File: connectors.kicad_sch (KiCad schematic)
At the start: 15 parts, among them J1 Compute-Module-4_Plug_Connect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, Q2 SQS401EN-T1_BE3, Q3 DZDH0401DW, U20 NTS0102_XSON, U21 NTS0102_XSON

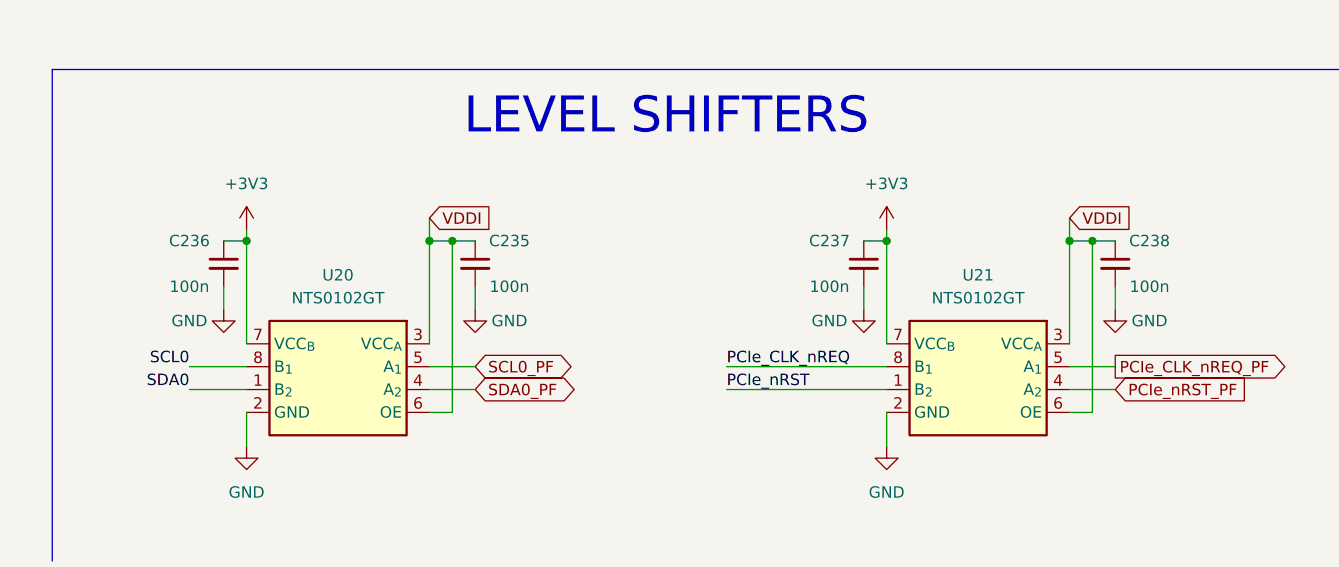
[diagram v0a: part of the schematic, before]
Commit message: [#55992] Replace 100n capacitors
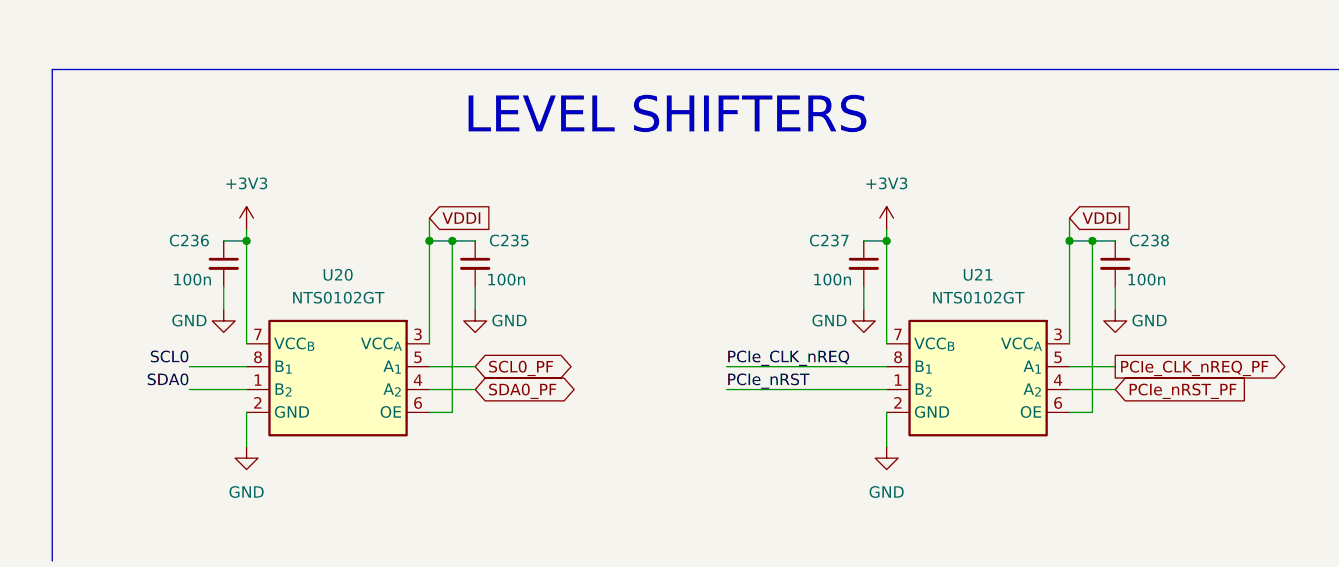
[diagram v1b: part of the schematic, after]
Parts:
- C235, C236, C237, C238: value C_100n_0201 -> C_100n_0402; footprint antmicro-footprints:C_0201 -> antmicro-footprints:C_0402_1005Metric; symbol antmicroCapacitorsmisc:C_100n_0201 -> antmicroCapacitors0402:C_100n_0402; Dielectric (none) -> X5R; MPN CC0201KRX6S5BB104 -> GRM155R61H104KE14D; Manufacturer YAGEO -> Murata; Voltage (none) -> 50V

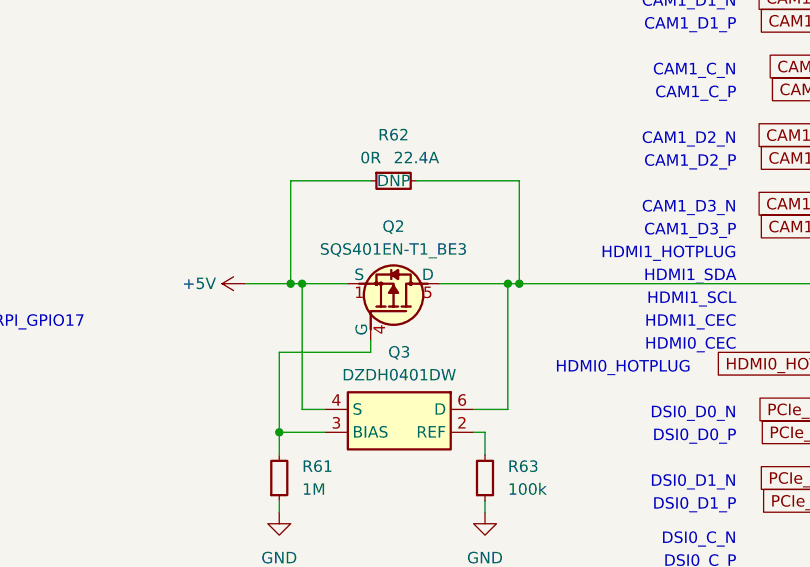
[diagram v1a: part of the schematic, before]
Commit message: [#56060] Connect power monitor and ideal diode
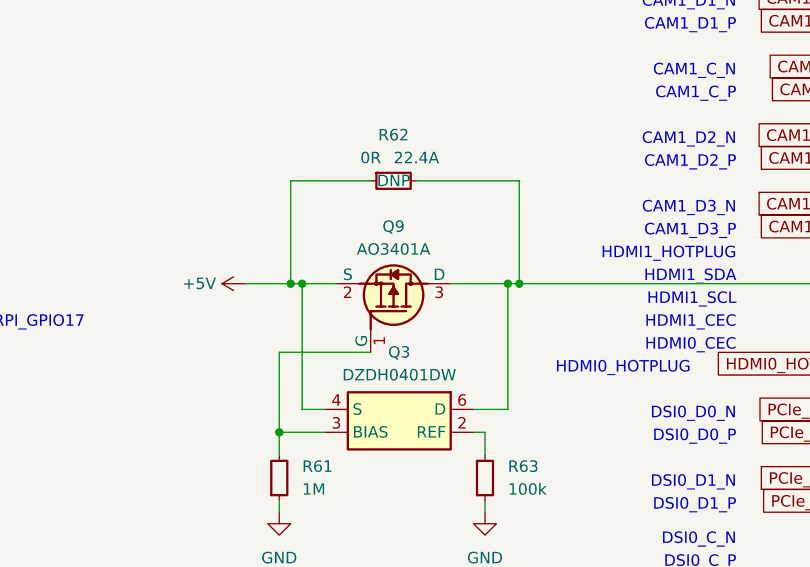
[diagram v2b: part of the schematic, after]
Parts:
- removed Q2: SQS401EN-T1_BE3, antmicro-footprints:Vishay_PowerPAK_1212-8_Single, symbol antmicroTransistorsFETsMOSFETsSingle:SQS401EN-T1_BE3
- added Q9: AO3401A, antmicro-footprints:SOT-23-3, symbol antmicroTransistorsFETsMOSFETsSingle:AO3401A
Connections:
- net +5V: now also Q9.2 (S)
- net at Q3.3 (BIAS), R61.2: now also Q9.1 (G)
- net at J1.143, J1.145, J1.147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: now also Q9.3 (D)
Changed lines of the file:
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@@
     (stroke (width 0) (type default))
   )
-  (wire (pts (xy 234.95 135.89) (xy 242.57 135.89))
-    (stroke (width 0) (type default))
-  )
   (wire (pts (xy 124.46 81.28) (xy 129.54 81.28))
     (stroke (width 0) (type default))
@@
     (stroke (width 0) (type default))
   )
+  (wire (pts (xy 236.22 135.89) (xy 242.57 135.89))
+    (stroke (width 0) (type default))
+  )
   (wire (pts (xy 220.98 247.65) (xy 220.98 259.08))
     (stroke (width 0) (type default))
@@
     (stroke (width 0) (type default))
   )
-  (wire (pts (xy 227.33 142.24) (xy 227.33 143.51))
-    (stroke (width 0) (type default))
-  )
   (wire (pts (xy 133.35 177.8) (xy 124.46 177.8))
     (stroke (width 0) (type default))
@@
     (stroke (width 0) (type default))
   )
-  (wire (pts (xy 219.71 135.89) (xy 224.79 135.89))
+  (wire (pts (xy 219.71 135.89) (xy 223.52 135.89))
     (stroke (width 0) (type default))
   )
@@
     )
   )
-  (symbol (lib_id "antmicroTransistorsFETsMOSFETsSingle:SQS401EN-T1_BE3") (at 227.33 142.24 270) (mirror x) (unit 1)
-    (in_bom no) (on_board yes) (dnp no)
-    (property "Reference" "Q2" (at 229.87 129.54 90)
-      (effects (font (size 1.27 1.27) (thickness 0.15)))
-    )
-    (property "Value" "SQS401EN-T1_BE3" (at 217.17 127 0)
-      (effects (font (size 1.27 1.27) (thickness 0.15)) (justify left bottom) hide)
-    )
-    (property "Footprint" "antmicro-footprints:Vishay_PowerPAK_1212-8_Single" (at 214.63 127 0)
-      (effects (font (size 1.27 1.27) (thickness 0.15)) (justify left bottom) hide)
-    )
-    (property "Datasheet" "https://www.vishay.com/docs/65529/sqs401en.pdf" (at 212.09 127 0)
-      (effects (font (size 1.27 1.27) (thickness 0.15)) (justify left bottom) hide)
-    )
-    (property "MPN" "SQS401EN-T1_BE3" (at 229.87 132.08 90)
-      (effects (font (size 1.27 1.27) (thickness 0.15)))
-    )
-    (property "Manufacturer" "Vishay" (at 209.55 127 0)
-      (effects (font (size 1.27 1.27) (thickness 0.15)) (justify left bottom) hide)
-    )
-    (property "Author" "Antmicro" (at 207.01 127 0)
-      (effects (font (size 1.27 1.27) (thickness 0.15)) (justify left bottom) hide)
-    )
-    (property "License" "Apache-2.0" (at 204.47 127 0)
-      (effects (font (size 1.27 1.27) (thickness 0.15)) (justify left bottom) hide)
-    )
-    (pin "3")
-    (pin "1")
-    (pin "4")
-    (pin "2")
-    (pin "5")
-    (instances
-      (project "polarfire-som"
-        (path "/db4a0d3e-2eb3-499e-977d-6eb378cfd3ed/1a89b4c6-5d95-4c13-8da9-62b42c0a8ed9"
-          (reference "Q2") (unit 1)
-        )
-      )
-    )
-  )
   (symbol (lib_id "antmicroResistors0603:R_10k_0603") (at 165.1 140.97 0) (unit 1)
     (in_bom yes) (on_board yes) (dnp no)
@@
         )
       )
+    )
+  )
+  (symbol (lib_id "antmicroTransistorsFETsMOSFETsSingle:AO3401A") (at 227.33 143.51 270) (mirror x) (unit 1)
+    (in_bom yes) (on_board yes) (dnp no)
+    (property "Reference" "Q9" (at 229.87 129.54 90)
+      (effects (font (size 1.27 1.27) (thickness 0.15)))
+    )
+    (property "Value" "AO3401A" (at 229.87 132.08 90)
+      (effects (font (size 1.27 1.27) (thickness 0.15)))
+    )
+    (property "Footprint" "antmicro-footprints:SOT-23-3" (at 215.9 120.65 0)
+      (effects (font (size 1.27 1.27) (thickness 0.15)) (justify left bottom) hide)
+    )
+    (property "Datasheet" "http://aosmd.com/res/data_sheets/AO3401A.pdf" (at 213.36 120.65 0)
+      (effects (font (size 1.27 1.27) (thickness 0.15)) (justify left bottom) hide)
+    )
+    (property "MPN" "AO3401A" (at 210.82 120.65 0)
+      (effects (font (size 1.27 1.27) (thickness 0.15)) (justify left bottom) hide)
+    )
+    (property "Manufacturer" "AOSMD" (at 208.28 120.65 0)
+      (effects (font (size 1.27 1.27) (thickness 0.15)) (justify left bottom) hide)
+    )
+    (property "Author" "Antmicro" (at 205.74 120.65 0)
+      (effects (font (size 1.27 1.27) (thickness 0.15)) (justify left bottom) hide)
+    )
+    (property "License" "Apache-2.0" (at 203.2 120.65 0)
+      (effects (font (size 1.27 1.27) (thickness 0.15)) (justify left bottom) hide)
+    )
+    (pin "2")
+    (pin "1")
+    (pin "3")
+    (instances
+      (project "polarfire-som"
+        (path "/db4a0d3e-2eb3-499e-977d-6eb378cfd3ed/1a89b4c6-5d95-4c13-8da9-62b42c0a8ed9"
+          (reference "Q9") (unit 1)
+        )
+      )

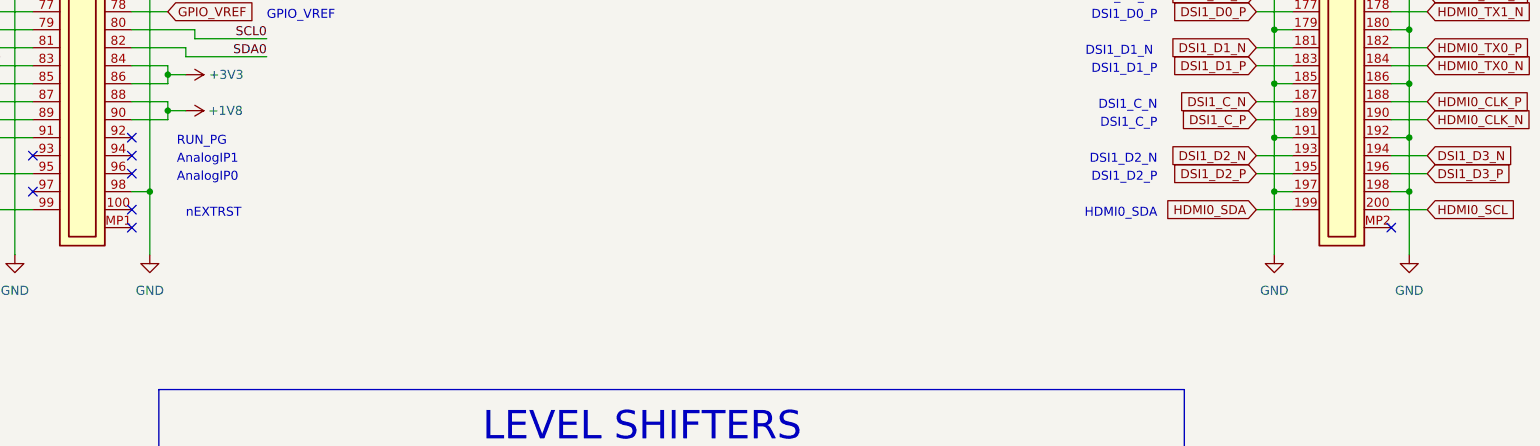
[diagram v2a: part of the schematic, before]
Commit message: [#56060] Finish PDN, continue routing LS signals
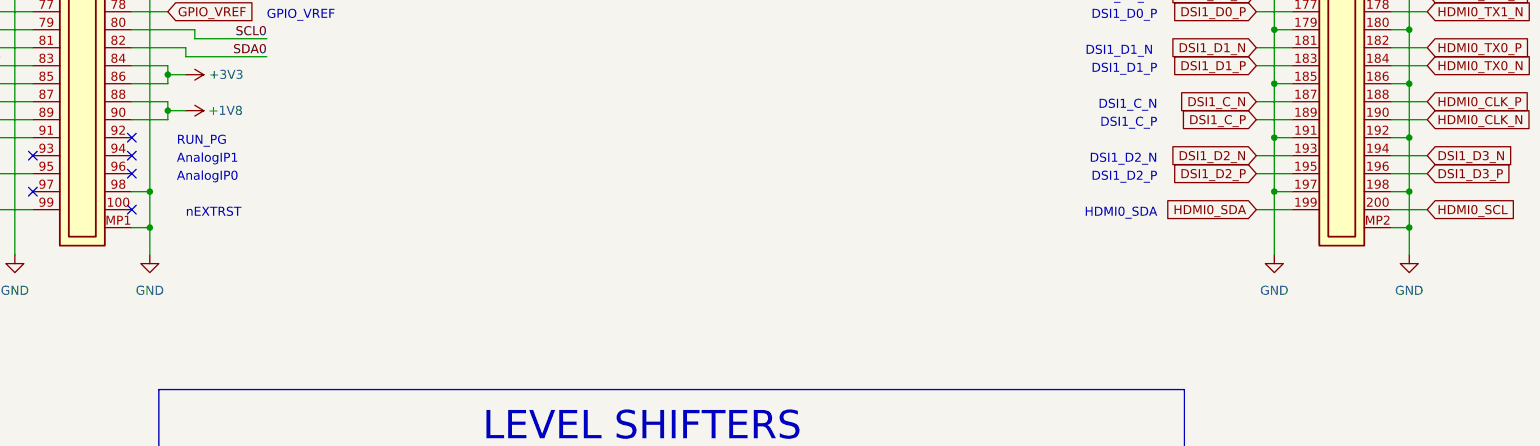
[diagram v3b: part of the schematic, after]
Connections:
- net GND: now also J1.MP1, J1.MP2
- no-connect marks 17 -> 15
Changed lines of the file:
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@@
   (junction (at 127 93.98) (diameter 0) (color 0 0 0 0)
   )
+  (junction (at 304.8 205.74) (diameter 0) (color 0 0 0 0)
+  )
   (junction (at 217.17 152.4) (diameter 0) (color 0 0 0 0)
   )
@@
   (junction (at 107.95 160.02) (diameter 0) (color 0 0 0 0)
   )
+  (junction (at 127 205.74) (diameter 0) (color 0 0 0 0)
+  )
   (junction (at 149.86 247.65) (diameter 0) (color 0 0 0 0)
   )
@@
   )
   (no_connect (at 302.26 83.82))
-  (no_connect (at 124.46 205.74))
   (no_connect (at 288.29 167.64))
   (no_connect (at 288.29 165.1))
@@
   (no_connect (at 124.46 203.2))
   (no_connect (at 124.46 172.72))
-  (no_connect (at 302.26 205.74))
   (no_connect (at 124.46 198.12))
   (no_connect (at 124.46 193.04))
@@
     (stroke (width 0) (type default))
   )
+  (wire (pts (xy 124.46 205.74) (xy 127 205.74))
+    (stroke (width 0) (type default))
+  )
   (wire (pts (xy 302.26 124.46) (xy 304.8 124.46))
     (stroke (width 0) (type default))
@@
     (stroke (width 0) (type default))
   )
+  (wire (pts (xy 304.8 205.74) (xy 304.8 209.55))
+    (stroke (width 0) (type default))
+  )
   (wire (pts (xy 124.46 132.08) (xy 129.54 132.08))
     (stroke (width 0) (type default))
@@
     (stroke (width 0) (type default))
   )
+  (wire (pts (xy 302.26 205.74) (xy 304.8 205.74))
+    (stroke (width 0) (type default))
+  )
   (wire (pts (xy 105.41 182.88) (xy 110.49 182.88))
     (stroke (width 0) (type default))
@@
     (stroke (width 0) (type default))
   )
-  (wire (pts (xy 304.8 200.66) (xy 304.8 209.55))
+  (wire (pts (xy 304.8 200.66) (xy 304.8 205.74))
     (stroke (width 0) (type default))
   )
@@
     (stroke (width 0) (type default))
   )
+  (wire (pts (xy 127 205.74) (xy 127 209.55))
+    (stroke (width 0) (type default))
+  )
   (wire (pts (xy 283.21 83.82) (xy 288.29 83.82))
     (stroke (width 0) (type default))
@@
     (stroke (width 0) (type default))
   )
-  (wire (pts (xy 127 200.66) (xy 127 209.55))
-    (stroke (width 0) (type default))
-  )
+  (wire (pts (xy 127 200.66) (xy 127 205.74))
+    (stroke (width 0) (type default))
+  )
